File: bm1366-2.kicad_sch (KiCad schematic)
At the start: 88 parts, among them U1 25MHz, U13 ADP171AUJ-R7, U18 TLV3544, U19 BM1366_mode0, U22 BM1366_mode0, U23 ADP171AUJ-R7

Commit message: change 1 ohm power resistors to 2 watt parts, changed schematic and BOM
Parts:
- R62, R68: DK 118-CR2512-F/-1R00ELFCT-ND -> CRM2512-JW-1R0ELFCT-ND; PARTNO CR2512-F/-1R00ELF -> CRM2512-JW-1R0ELF
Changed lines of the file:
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@@
       (effects (font (size 1.27 1.27)) hide)
     )
-    (property "DK" "118-CR2512-F/-1R00ELFCT-ND" (at 121.285 179.705 0)
-      (effects (font (size 1.27 1.27)) hide)
-    )
-    (property "PARTNO" "CR2512-F/-1R00ELF" (at 121.285 179.705 0)
+    (property "DK" "CRM2512-JW-1R0ELFCT-ND" (at 121.285 179.705 0)
+      (effects (font (size 1.27 1.27)) hide)
+    )
+    (property "PARTNO" "CRM2512-JW-1R0ELF" (at 121.285 179.705 0)
       (effects (font (size 1.27 1.27)) hide)
     )
@@
       (effects (font (size 1.27 1.27)) hide)
     )
-    (property "DK" "118-CR2512-F/-1R00ELFCT-ND" (at 130.175 179.705 0)
-      (effects (font (size 1.27 1.27)) hide)
-    )
-    (property "PARTNO" "CR2512-F/-1R00ELF" (at 130.175 179.705 0)
-      (effects (font (size 1.27 1.27)) hide)
-    )
+    (property "DK" "CRM2512-JW-1R0ELFCT-ND" (at 130.175 179.705 0)
+      (effects (font (size 1.27 1.27)) hide)
+    )
+    (property "PARTNO" "CRM2512-JW-1R0ELF" (at 130.175 179.705 0)
+      (effects (font (size 1.27 1.27)) hide)
+    )

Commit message: Start working on changelist for v301
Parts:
- R6: value 1k -> 10k
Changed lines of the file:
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@@
       (effects (font (size 1.27 1.27)))
     )
-    (property "Value" "1k" (at 37.465 47.625 90)
+    (property "Value" "10k" (at 37.465 47.625 90)
       (effects (font (size 1.27 1.27)))
     )

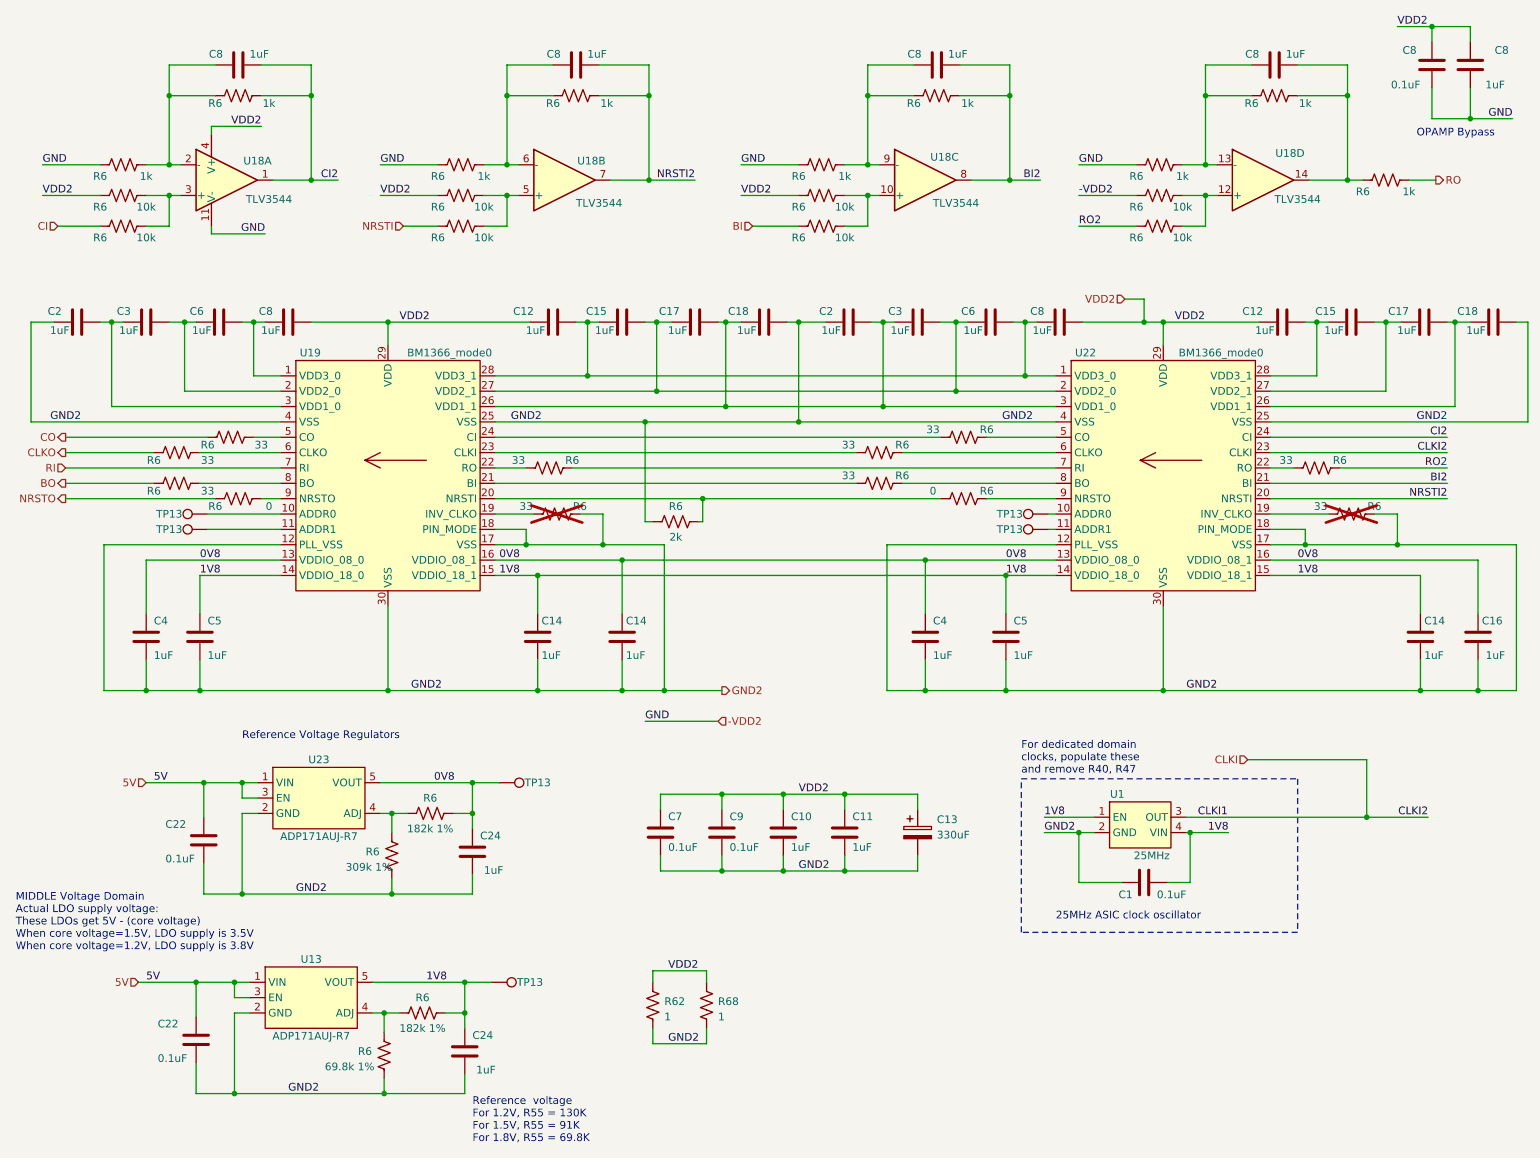
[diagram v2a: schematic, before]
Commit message: remove old 5V power supply, prepare footprints for new 5V buck supply, switch fans to 12V
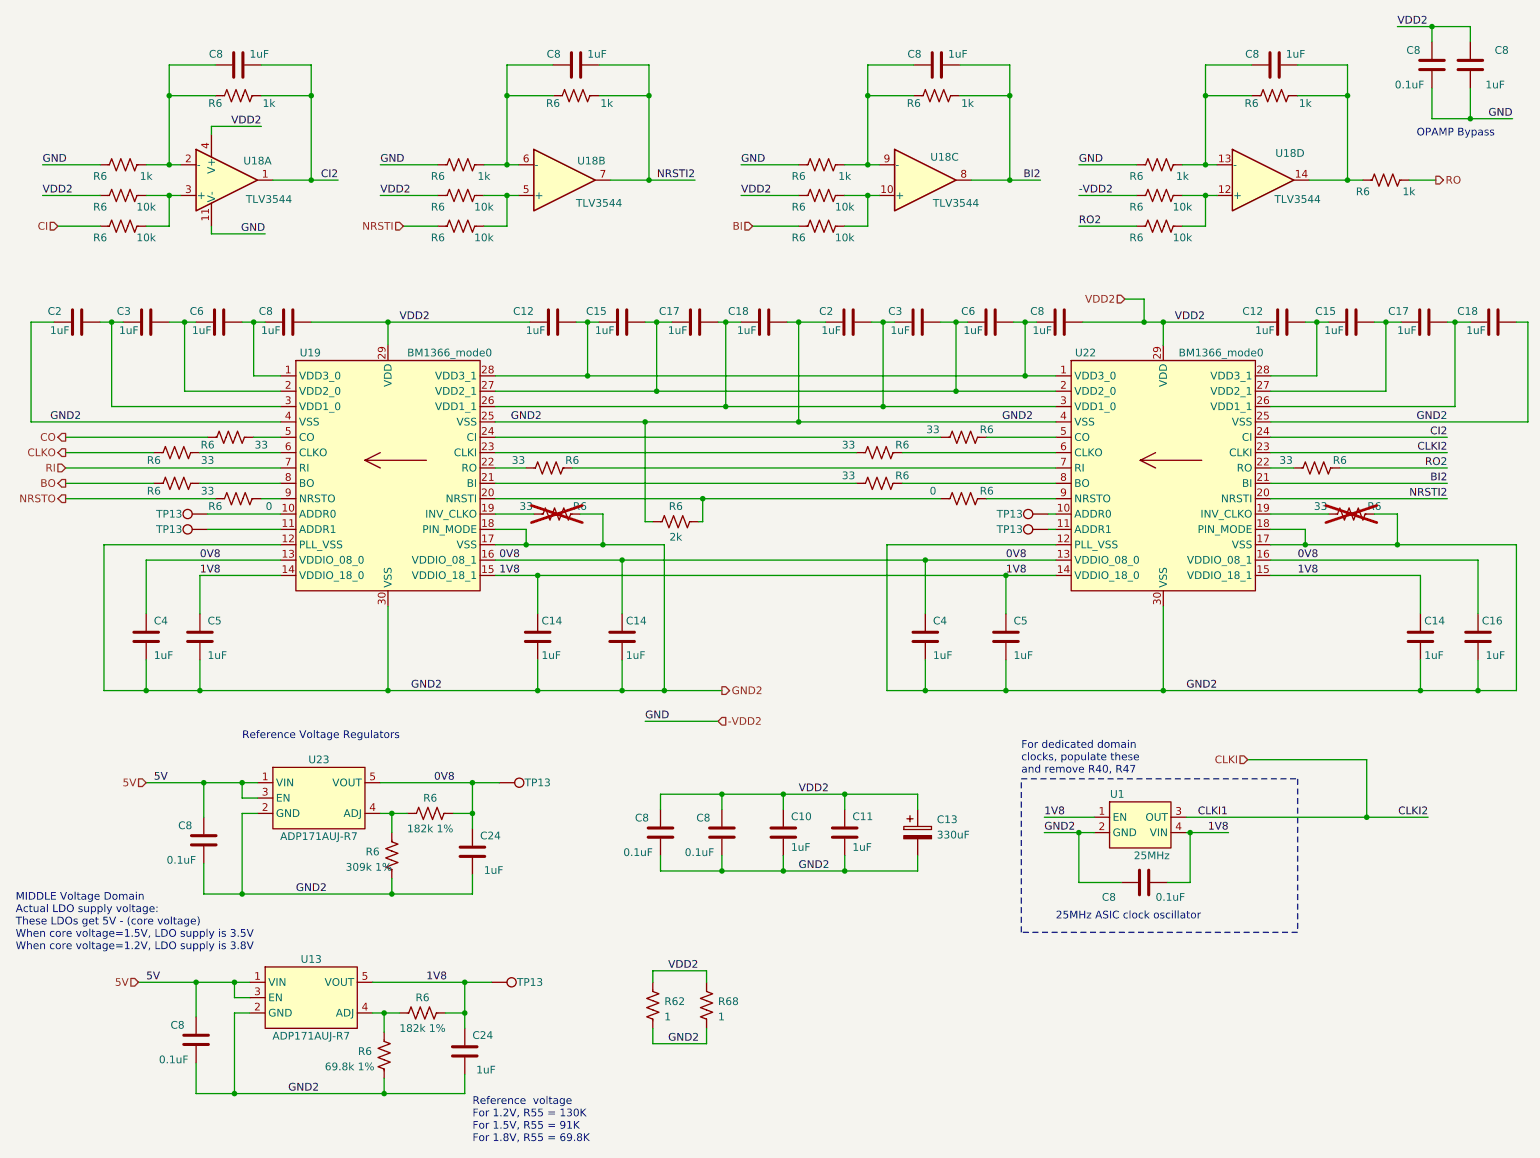
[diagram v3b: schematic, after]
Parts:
- removed C1, C22 (x2), C7, C8, C9: 0.1uF, Capacitor_SMD:C_0402_1005Metric, symbol Device:C
- added C8 (x6): 0.1uF, Capacitor_SMD:C_0402_1005Metric, symbol Device:C
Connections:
- net -VDD2: now also C8.1
- net 1V8: now also C8.1
- net 5V: now also C8.2, C8.2
- net GND2: now also C8.1, C8.1, C8.1, C8.1, C8.2
- net VDD2: now also C8.2, C8.2, C8.2

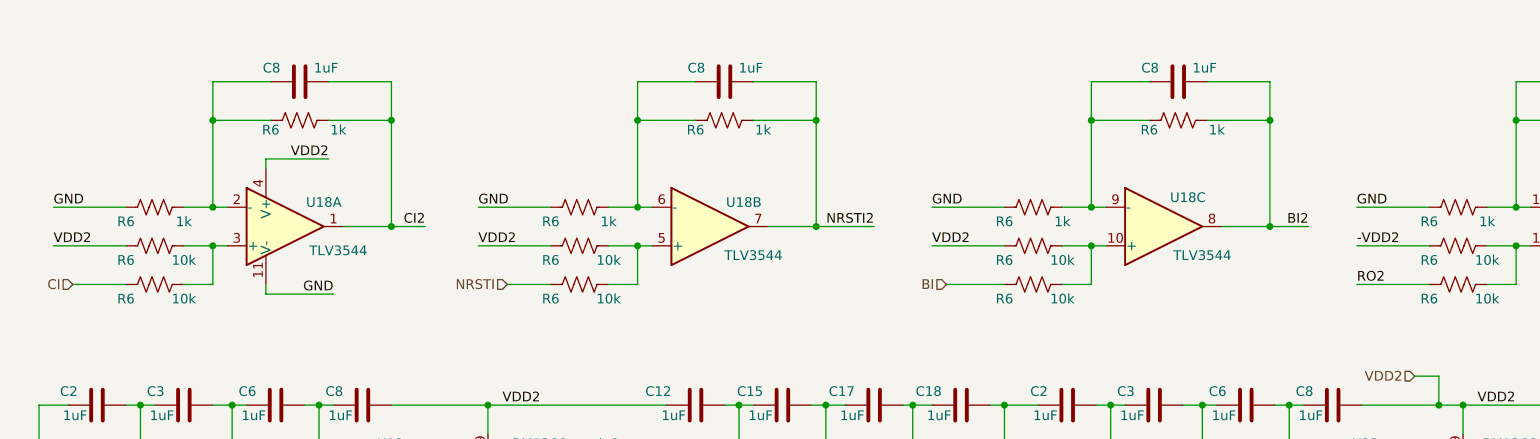
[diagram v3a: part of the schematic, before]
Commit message: Fix level translator negative input
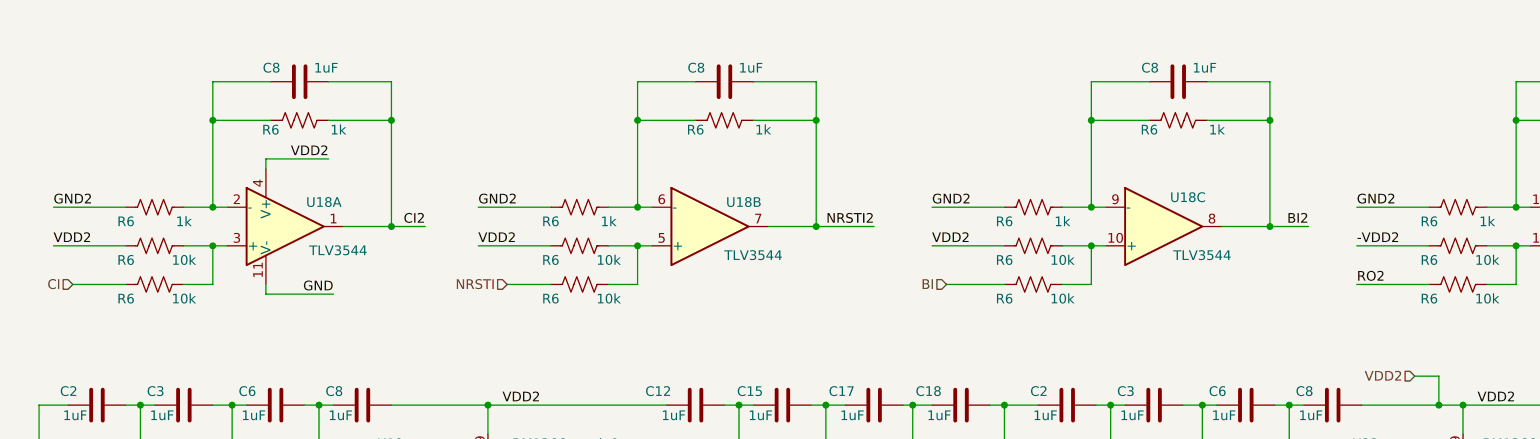
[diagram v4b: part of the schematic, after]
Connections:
- net -VDD2: no longer R6.2, R6.2, R6.2, R6.2
- net GND2: now also R6.2, R6.2, R6.2, R6.2
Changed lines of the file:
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@@
     (effects (font (size 1.27 1.27)) (justify right bottom))
   )
-  (label "GND" (at 135.89 40.64 0) (fields_autoplaced)
+  (label "GND2" (at 135.89 40.64 0) (fields_autoplaced)
     (effects (font (size 1.27 1.27)) (justify left bottom))
   )
@@
     (effects (font (size 1.27 1.27)) (justify right bottom))
   )
-  (label "GND" (at 76.2 40.64 0) (fields_autoplaced)
+  (label "GND2" (at 76.2 40.64 0) (fields_autoplaced)
     (effects (font (size 1.27 1.27)) (justify left bottom))
   )
@@
     (effects (font (size 1.27 1.27)) (justify left bottom))
   )
-  (label "GND" (at 20.32 40.64 0) (fields_autoplaced)
+  (label "GND2" (at 20.32 40.64 0) (fields_autoplaced)
     (effects (font (size 1.27 1.27)) (justify left bottom))
   )
@@
     (effects (font (size 1.27 1.27)) (justify right bottom))
   )
-  (label "GND" (at 191.77 40.64 0) (fields_autoplaced)
+  (label "GND2" (at 191.77 40.64 0) (fields_autoplaced)
     (effects (font (size 1.27 1.27)) (justify left bottom))
   )

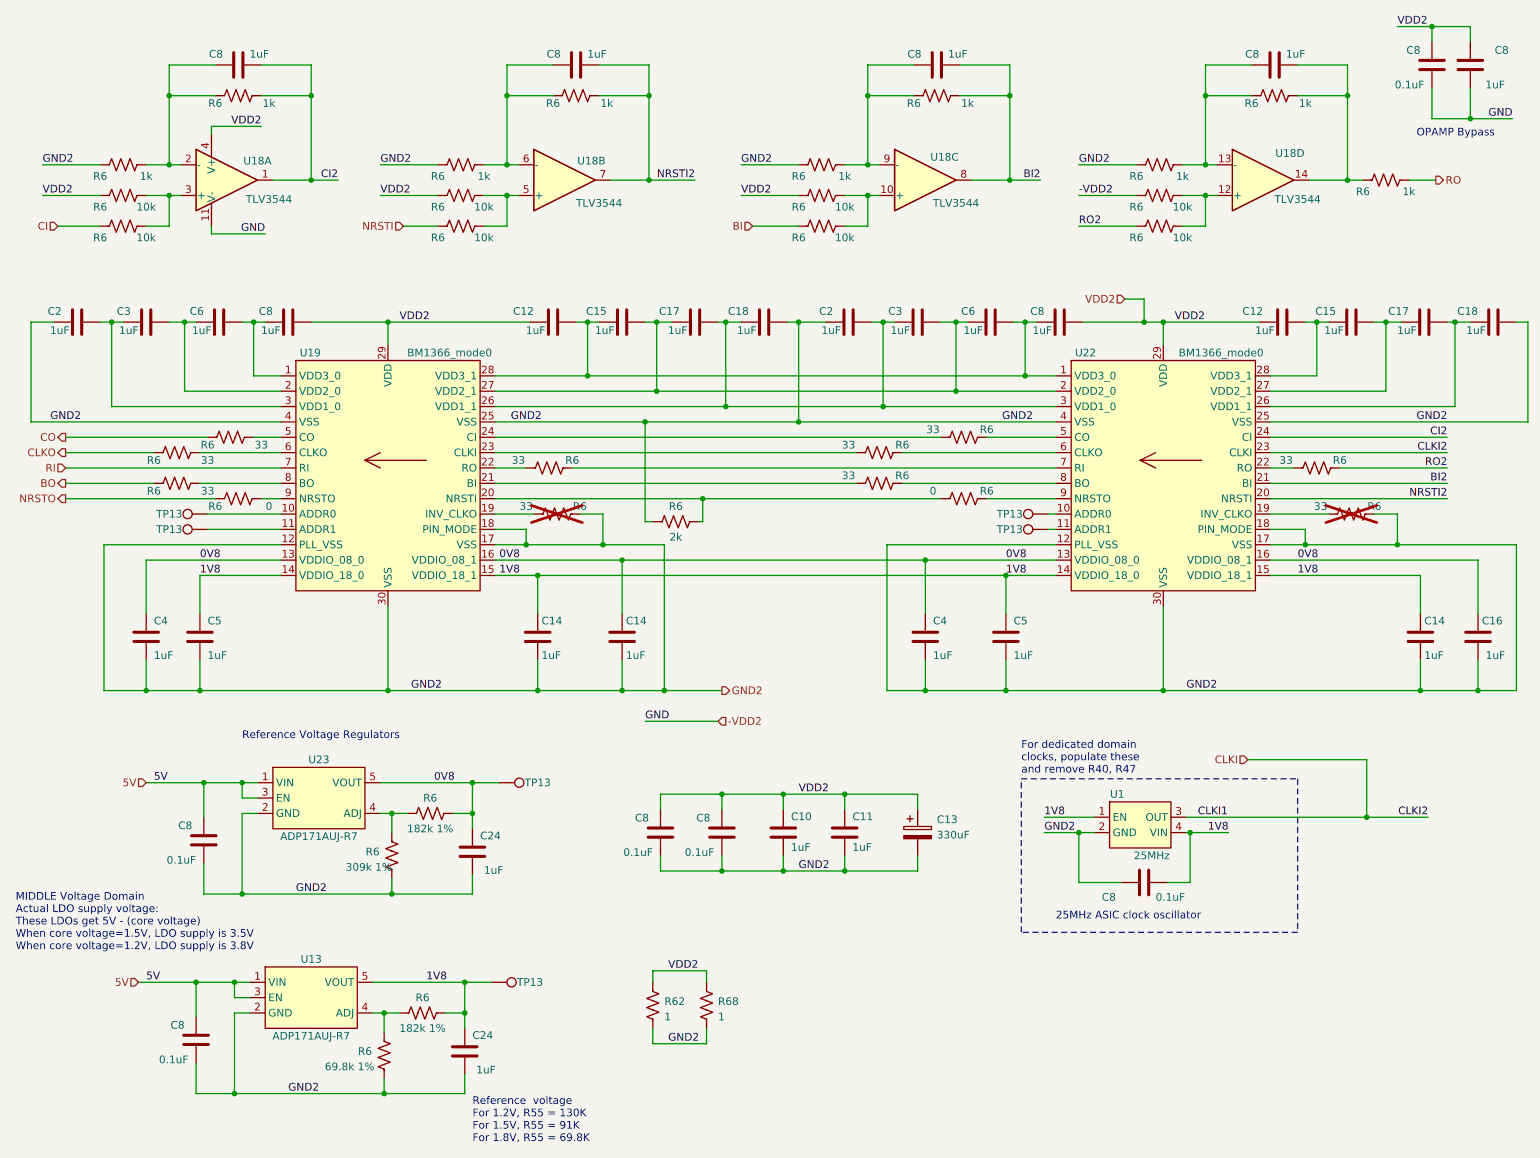
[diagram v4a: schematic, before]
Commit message: Finished routing, generate gerbers, edit new BOM for v301
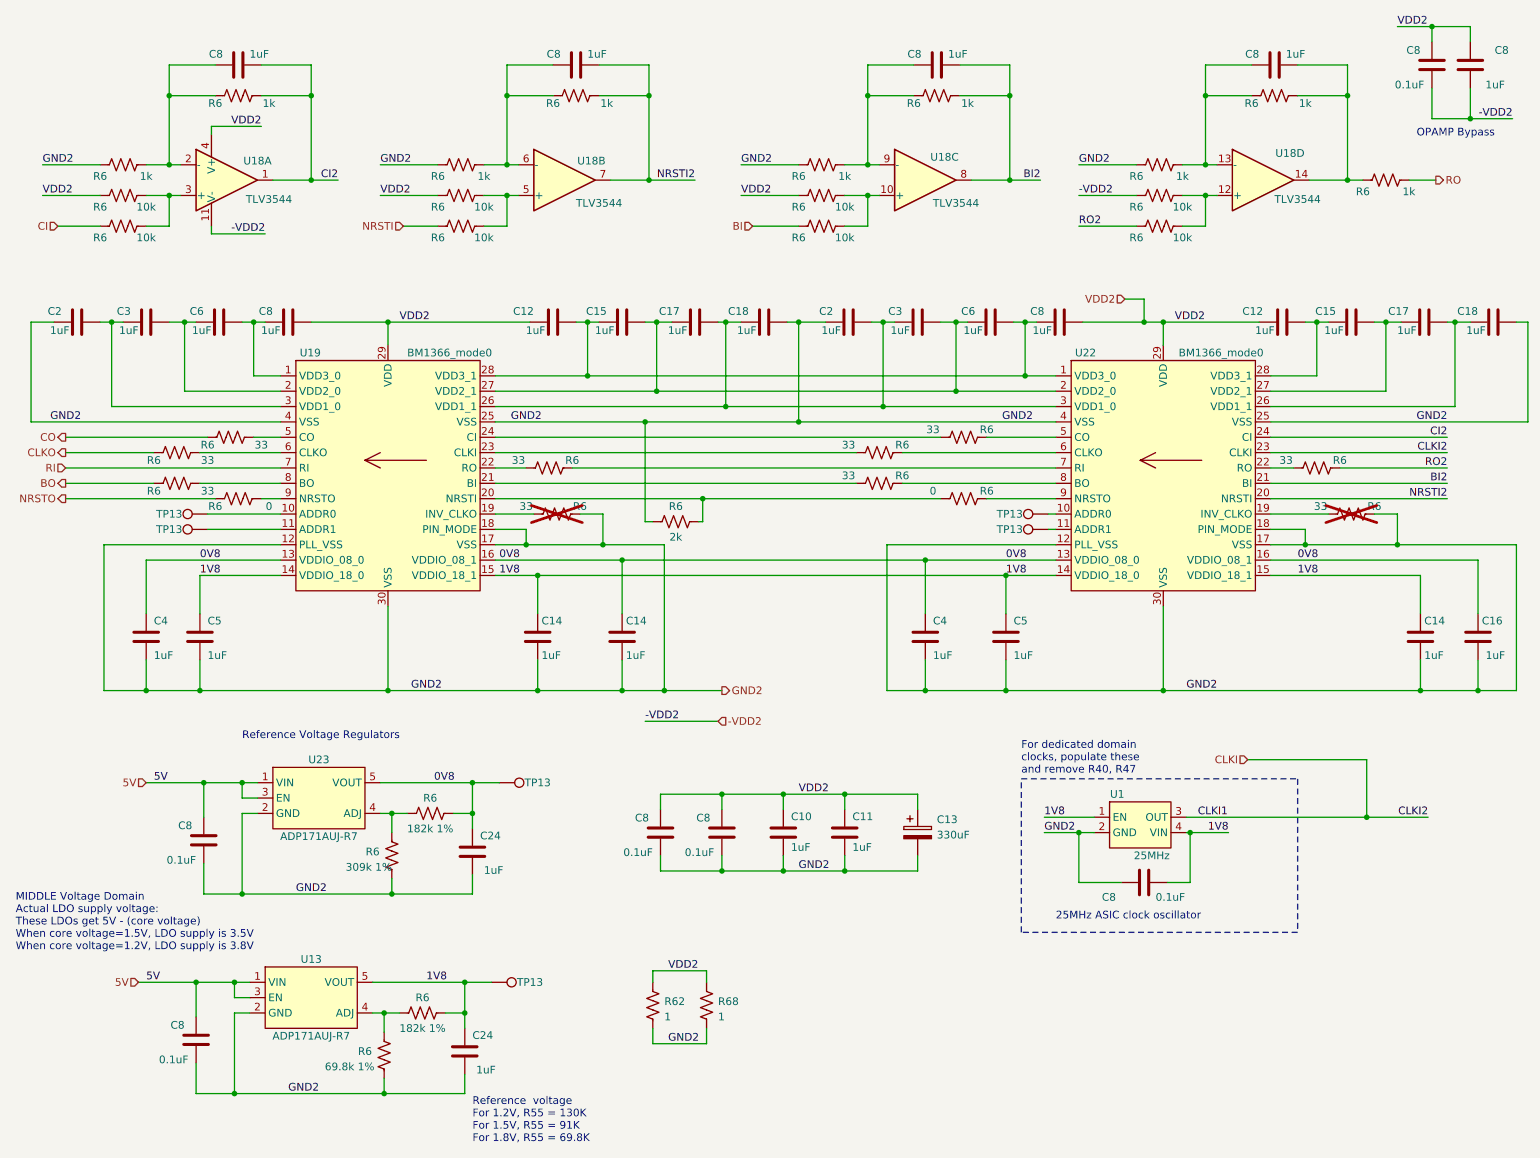
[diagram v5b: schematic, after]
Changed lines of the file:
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@@
     (effects (font (size 1.27 1.27)) (justify left bottom))
   )
-  (label "GND" (at 57.15 52.07 180) (fields_autoplaced)
+  (label "-VDD2" (at 57.15 52.07 180) (fields_autoplaced)
     (effects (font (size 1.27 1.27)) (justify right bottom))
   )
@@
     (effects (font (size 1.27 1.27)) (justify left bottom))
   )
-  (label "GND" (at 120.015 132.715 0) (fields_autoplaced)
+  (label "-VDD2" (at 120.015 132.715 0) (fields_autoplaced)
     (effects (font (size 1.27 1.27)) (justify left bottom))
   )
@@
     (effects (font (size 1.27 1.27)) (justify left bottom))
   )
-  (label "GND" (at 263.525 33.02 180) (fields_autoplaced)
+  (label "-VDD2" (at 263.525 33.02 180) (fields_autoplaced)
     (effects (font (size 1.27 1.27)) (justify right bottom))
   )

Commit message: BOM cleanup
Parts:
- R6: DK 311-1.00KLRCT-ND -> 311-10KJRCT-ND; PARTNO RC0402FR-071KL -> RC0402JR-0710KL
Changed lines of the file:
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@@
       (effects (font (size 1.27 1.27)) hide)
     )
-    (property "DK" "311-1.00KLRCT-ND" (at 33.655 45.72 0)
+    (property "DK" "311-10KJRCT-ND" (at 33.655 45.72 0)
       (effects (font (size 1.27 1.27)) hide)
     )
-    (property "PARTNO" "RC0402FR-071KL" (at 33.655 45.72 0)
+    (property "PARTNO" "RC0402JR-0710KL" (at 33.655 45.72 0)
       (effects (font (size 1.27 1.27)) hide)
     )
